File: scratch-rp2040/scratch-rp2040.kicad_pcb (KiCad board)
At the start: 2 copper layers, 32 parts, among them P1 USB_C_Plug_USB2.0, SW1 SW_SPST, SW2 SW_SPST, SW3 SW_SPST, SW4 SW_SPST, SW5 SW_SPST, SW6 SW_SPST, SW7 SW_SPST, U1 RP2040, U2 NCP1117-3.3_SOT223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

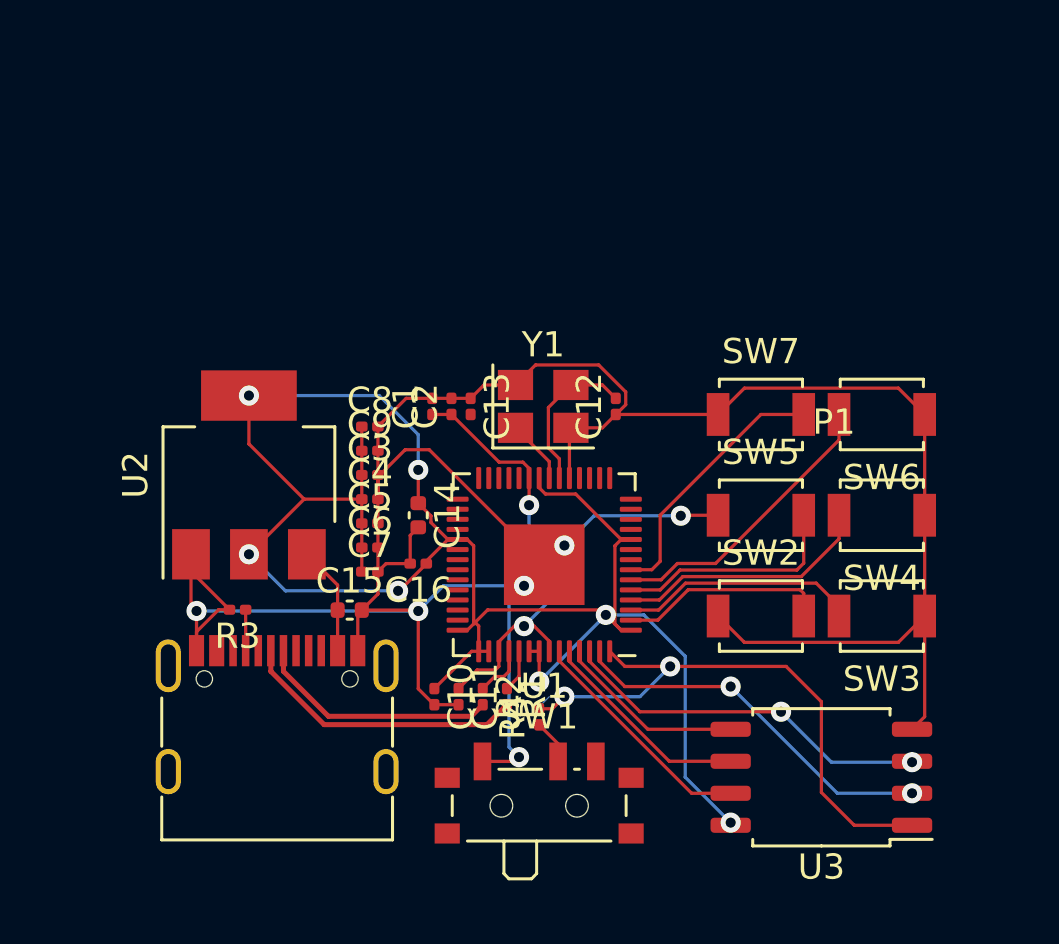
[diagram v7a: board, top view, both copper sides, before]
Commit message: wired GPIOs remained
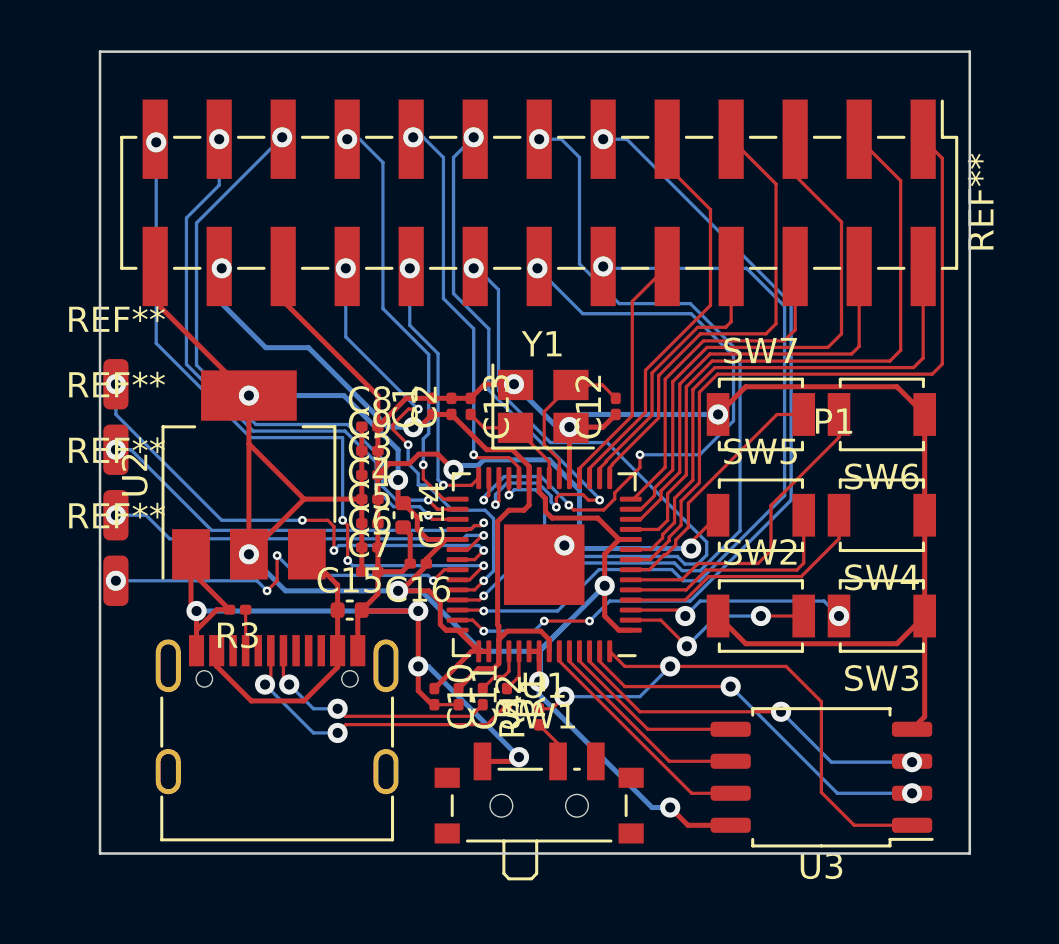
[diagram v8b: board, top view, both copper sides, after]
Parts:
- added REF**: SolderWirePad_1x01_SMD_1x2mm, Connector_Wire:SolderWirePad_1x01_SMD_1x2mm, F.Cu at (51.2, 33.2)
- added REF**: SolderWirePad_1x01_SMD_1x2mm, Connector_Wire:SolderWirePad_1x01_SMD_1x2mm, F.Cu at (51.2, 35.8)
- added REF**: SolderWirePad_1x01_SMD_1x2mm, Connector_Wire:SolderWirePad_1x01_SMD_1x2mm, F.Cu at (51.2, 41.0)
- added REF**: PinHeader_2x13_P2.54mm_Vertical_SMD, Connector_PinHeader_2.54mm:PinHeader_2x13_P2.54mm_Vertical_SMD, F.Cu at (68.0, 26.0)
- added REF**: SolderWirePad_1x01_SMD_1x2mm, Connector_Wire:SolderWirePad_1x01_SMD_1x2mm, F.Cu at (51.2, 38.4)
- moved C14 0.60 mm to (62.6, 38.4)
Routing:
- net unconnected-(U1-GPIO27_ADC1-Pad39): track 0.00 -> 34.0 mm, vias 0 -> 2
- net unconnected-(U1-GPIO29_ADC3-Pad41): track 0.00 -> 33.5 mm, vias 0 -> 4
- net unconnected-(U1-GPIO28_ADC2-Pad40): track 0.00 -> 30.6 mm, vias 0 -> 2
- net unconnected-(U1-GPIO25-Pad37): track 0.00 -> 28.8 mm, vias 0 -> 4
- net unconnected-(U1-SWD-Pad25): track 0.00 -> 28.4 mm, vias 0 -> 2
- net unconnected-(U1-GPIO6-Pad8): track 0.00 -> 27.6 mm
- net +3.3V: track 78.7 -> 104.6 mm
- net unconnected-(U1-GPIO16-Pad27): track 0.00 -> 25.7 mm, vias 0 -> 4
- net unconnected-(U1-GPIO8-Pad11): track 0.00 -> 25.4 mm
- net unconnected-(U1-RUN-Pad26): track 0.00 -> 24.1 mm, vias 0 -> 4
- net unconnected-(U1-GPIO19-Pad30): track 0.00 -> 23.8 mm, vias 0 -> 2
- net unconnected-(U1-GPIO20-Pad31): track 0.00 -> 23.4 mm, vias 0 -> 2
- net unconnected-(U1-GPIO10-Pad13): track 0.00 -> 22.0 mm
- net unconnected-(U1-GPIO7-Pad9): track 0.00 -> 21.1 mm
- net unconnected-(U1-GPIO23-Pad35): track 0.00 -> 19.9 mm, vias 0 -> 4
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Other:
- board outline added: 34.5 x 31.8 mm
